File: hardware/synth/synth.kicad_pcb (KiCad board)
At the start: 2 copper layers, 91.4 x 81.3 mm, 54 parts, among them J1 MIDI In, J2 MIDI Out, J3 Audio In, J4 AVR-UPDI-6, J5 Audio Out, SW1 POWER, U1 TLP2312, U2 ATtiny814-SS, U3 MCP6044, U4 MCP6042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

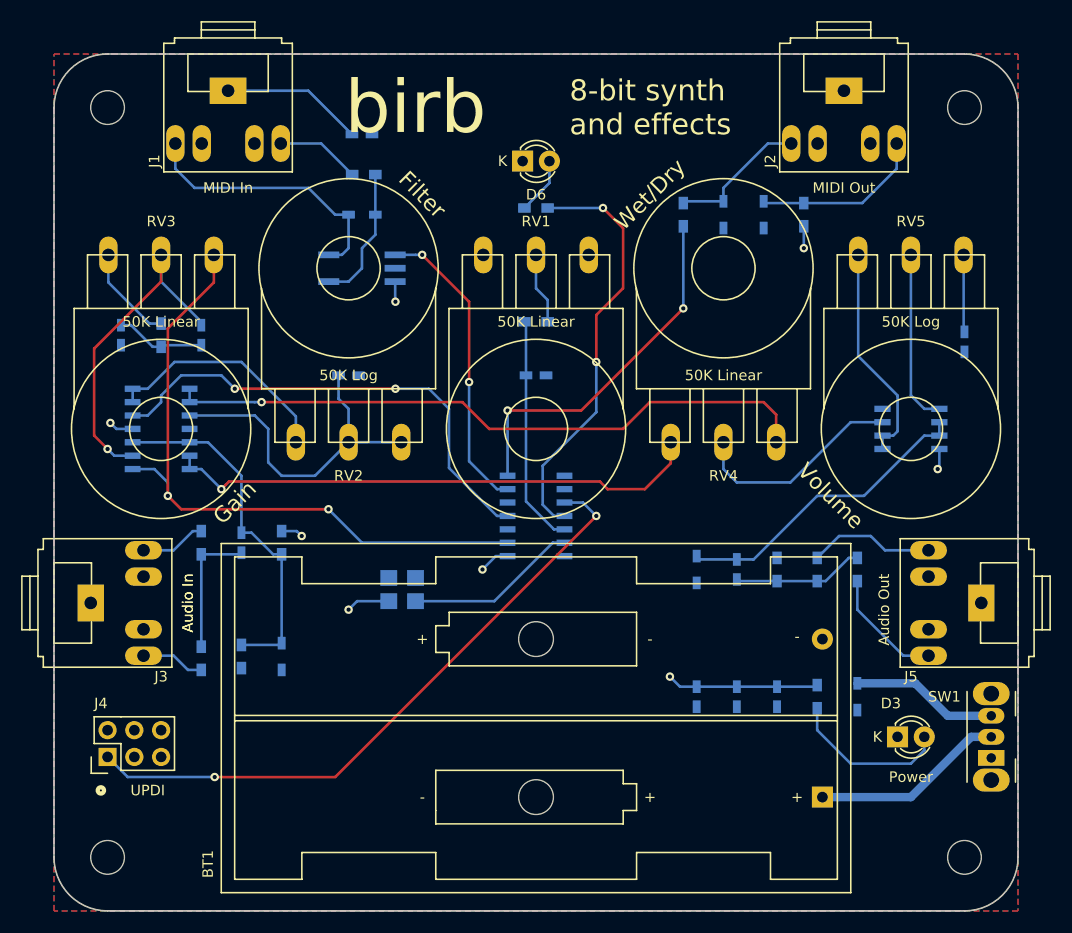
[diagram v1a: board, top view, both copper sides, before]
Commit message: Add selector switch PCB
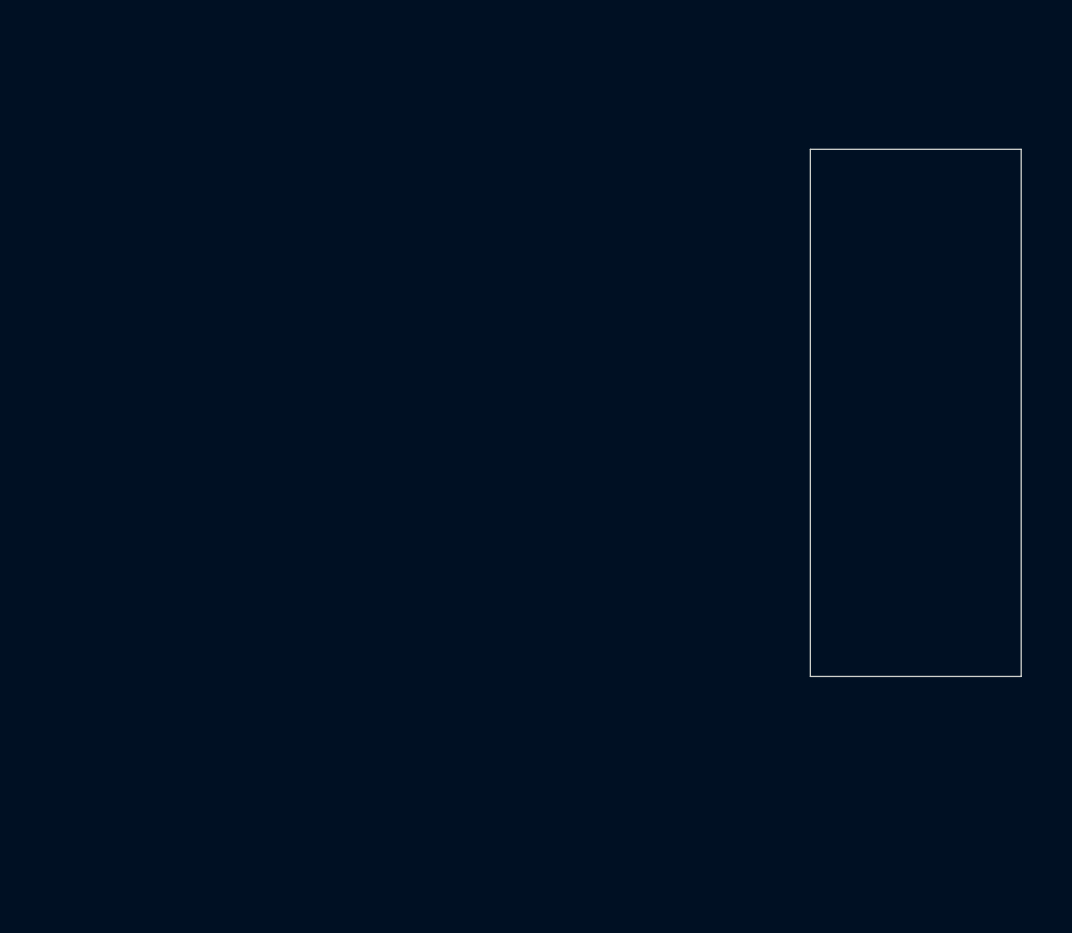
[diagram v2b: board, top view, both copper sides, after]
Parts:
- removed BT1: Battery, Battery:BatteryHolder_Keystone_2462_2xAA
- removed C1: 10u, Capacitors_SMD:C_0603_HandSoldering
- removed C10, C11, C6, C9: 1u, Capacitors_SMD:C_0603_HandSoldering
- removed C2, C4: 100n, Capacitors_SMD:C_0603_HandSoldering
- removed C3: 1n, Capacitors_SMD:C_0603_HandSoldering
- removed C5, C8: DNL, Capacitors_SMD:C_0603_HandSoldering
- removed C7: 10n, Capacitors_SMD:C_0603_HandSoldering
- removed D1, D2, D4, D5, D7, D8: TVS, synth:SOD-323-handsoldering
- removed D3: POWER, LEDs:LED-3MM
- removed D6: LED, LEDs:LED-3MM
- removed J1: MIDI In, synth:Tayda_3.5mm_stereo_TRS_jack_A-853
- removed J2: MIDI Out, synth:Tayda_3.5mm_stereo_TRS_jack_A-853
- removed J3: Audio In, synth:Tayda_3.5mm_stereo_TRS_jack_A-853
- removed J4: AVR-UPDI-6, Pin_Headers:Pin_Header_Straight_2x03
- removed J5: Audio Out, synth:Tayda_3.5mm_stereo_TRS_jack_A-853
- removed R1, R2, R6: 220R, Resistors_SMD:R_0603_HandSoldering
- removed R10, R13, R8: 1M, Resistors_SMD:R_0603_HandSoldering
- removed R11: 100R, Resistors_SMD:R_0603_HandSoldering
- removed R12, R14: 0R, Resistors_SMD:R_0603_HandSoldering
- removed R3, R5: 10R, Resistors_SMD:R_0603_HandSoldering
- removed R4: 100K, Resistors_SMD:R_0603_HandSoldering
- removed R7, R9: 10K, Resistors_SMD:R_0603_HandSoldering
- removed REF** (x4): MountingHole_3.2mm_M3, Mounting_Holes:MountingHole_3.2mm_M3
- removed RV1, RV3, RV4: 50K LIN, synth:Alpha_16mm_Potentiometer_RA
- removed RV2, RV5: 50K LOG, synth:Alpha_16mm_Potentiometer_RA
- removed SW1: POWER, Button_Switch_THT:SW_CuK_OS102011MA1QN1_SPDT_Angled
- removed U1: TLP2312, Package_SO:SO-5_4.4x3.6mm_P1.27mm
- removed U2: ATtiny814-SS, Housings_SOIC:SOIC-14_3.9x8.7mm_Pitch1.27mm
- removed U3: MCP6044, Housings_SOIC:SOIC-14_3.9x8.7mm_Pitch1.27mm
- removed U4: MCP6042, Housings_SOIC:SOIC-8_3.9x4.9mm_Pitch1.27mm
- removed X1: DSC1001, synth:DSC_1001_Oscillator_SMD_5032_4Pads
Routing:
- net /ADC: track 63.9 -> 0.00 mm, vias 2 -> 0
- net Net-(RV4-Pad3): track 62.1 -> 0.00 mm, vias 1 -> 0
- net /UPDI: track 60.9 -> 0.00 mm, vias 2 -> 0
- net Net-(RV4-Pad1): track 51.3 -> 0.00 mm, vias 1 -> 0
- net /DAC: track 46.3 -> 0.00 mm, vias 2 -> 0
- net VDD: track 45.9 -> 0.00 mm, vias 8 -> 0
- net /LED: track 40.4 -> 0.00 mm, vias 2 -> 0
- net /MIDI_OUT: track 34.7 -> 0.00 mm, vias 2 -> 0
- net Net-(C6-Pad1): track 34.0 -> 0.00 mm
- net Net-(C8-Pad1): track 32.4 -> 0.00 mm, vias 1 -> 0
- net Net-(C7-Pad1): track 32.4 -> 0.00 mm
- net Net-(C10-Pad2): track 29.3 -> 0.00 mm
- net /MIDI_IN: track 28.7 -> 0.00 mm, vias 2 -> 0
- net Net-(D2-Pad2): track 25.9 -> 0.00 mm
- net Net-(RV2-Pad1): track 22.4 -> 0.00 mm
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- removed copper zone on B.Cu, net GND
- removed copper zone on F.Cu, net VDD
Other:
- board size 91.4 x 81.3 mm -> 20 x 50 mm
- board text removed: "50K Linear"
- board text removed: "50K Log"
- board text removed: "8-bit synth and effects"
- board text removed: "Audio In"
- board text removed: "Audio Out"
- board text removed: "Filter"
- board text removed: "Gain"
- board text removed: "MIDI In"
- board text removed: "MIDI Out"
- board text removed: "Power"
- board text removed: "R"
- board text removed: "S"
- board text removed: "T"
- board text removed: "UPDI"
- board text removed: "Volume"
- board text removed: "Wet/Dry"
- board text removed: "birb"
- board text removed: "rev 1 by Eric Van Albert"

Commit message: Hardware rev 2 and some firmware updates
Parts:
- added BT1: Battery, Pin_Headers:Pin_Header_Straight_1x02, F.Cu at (122.2, 110.0)
- added C1: 10u, Capacitors_SMD:C_0805_HandSoldering, B.Cu at (131.5, 111.5)
- added C10: 47U, Capacitors_SMD:C_1210_HandSoldering, B.Cu at (136.0, 87.5)
- added C11: 100n, Capacitors_SMD:C_0603_HandSoldering, B.Cu at (122.8, 77.0)
- added C12: 100n, Capacitors_SMD:C_0603_HandSoldering, B.Cu at (132.8, 77.0)
- added C13: 100n, Capacitors_SMD:C_0603_HandSoldering, B.Cu at (122.8, 72.0)
- added C2: 100n, Capacitors_SMD:C_0603_HandSoldering, B.Cu at (127.5, 111.5)
- added C3: 1U, Capacitors_SMD:C_0603_HandSoldering, B.Cu at (133.0, 72.0)
- added C4: 1n, Capacitors_SMD:C_0603_HandSoldering, B.Cu at (129.5, 111.5)
- added C5: 1U, Capacitors_SMD:C_0603_HandSoldering, B.Cu at (125.0, 91.5)
- added C6: DNL, Capacitors_SMD:C_0603_HandSoldering, B.Cu at (132.5, 115.0)
- added C7: 47U, Capacitors_SMD:C_1210_HandSoldering, B.Cu at (124.0, 84.0)
- added C8: 47U, Capacitors_SMD:C_1210_HandSoldering, B.Cu at (124.0, 87.5)
- added C9: 47U, Capacitors_SMD:C_1210_HandSoldering, B.Cu at (136.0, 84.0)
- added D1: TVS, synth:SOD-323-handsoldering, B.Cu at (125.5, 111.3)
- added D2: POWER, LEDs:LED-5MM, F.Cu at (123.5, 106.5)
- added D3: LED, LEDs:LED-5MM, F.Cu at (136.5, 106.5)
- added D4: TVS, synth:SOD-323-handsoldering, B.Cu at (128.8, 88.0)
- added D5: TVS, synth:SOD-323-handsoldering, B.Cu at (131.2, 88.0)
- added D6: TVS, synth:SOD-323-handsoldering, B.Cu at (128.0, 115.0)
- added J1: TTL_MIDI_OUT, Pin_Headers:Pin_Header_Straight_1x01, F.Cu at (138.0, 97.2)
- added J2: MIDI In, Pin_Headers:Pin_Header_Straight_1x03, F.Cu at (127.5, 118.0)
- added J3: Audio Out, Pin_Headers:Pin_Header_Straight_1x03, F.Cu at (127.5, 67.2)
- added J4: UPDI, Pin_Headers:Pin_Header_Straight_1x02, F.Cu at (137.8, 110.0)
- added R1: 22K, Resistors_SMD:R_0603_HandSoldering, B.Cu at (128.5, 83.8)
- added R10: 100K, Resistors_SMD:R_0603_HandSoldering, B.Cu at (127.2, 77.0)
- added R11: 100K, Resistors_SMD:R_0603_HandSoldering, B.Cu at (137.2, 77.0)
- added R12: 100K, Resistors_SMD:R_0603_HandSoldering, B.Cu at (127.2, 72.0)
- added R2: 22K, Resistors_SMD:R_0603_HandSoldering, B.Cu at (131.5, 83.8)
- added R3: 220R, Resistors_SMD:R_0603_HandSoldering, B.Cu at (126.0, 105.2)
- added R4: 220R, Resistors_SMD:R_0603_HandSoldering, B.Cu at (134.2, 105.0)
- added R5: 18K, Resistors_SMD:R_0603_HandSoldering, B.Cu at (123.0, 93.0)
- added R6: 18K, Resistors_SMD:R_0603_HandSoldering, B.Cu at (135.8, 92.0)
- added R7: 220R, Resistors_SMD:R_0603_HandSoldering, B.Cu at (133.5, 111.5)
- added R8: 1M, Resistors_SMD:R_0603_HandSoldering, B.Cu at (127.5, 70.0)
- added R9: 1M, Resistors_SMD:R_0603_HandSoldering, B.Cu at (132.5, 70.0)
- added REF**: MountingHole_2.2mm_M2, Mounting_Holes:MountingHole_2.2mm_M2, F.Cu at (123.0, 117.0)
- added REF**: MountingHole_2.2mm_M2, Mounting_Holes:MountingHole_2.2mm_M2, F.Cu at (123.0, 68.0)
- added REF**: MountingHole_2.2mm_M2, Mounting_Holes:MountingHole_2.2mm_M2, F.Cu at (137.0, 68.0)
- added REF**: MountingHole_2.2mm_M2, Mounting_Holes:MountingHole_2.2mm_M2, F.Cu at (137.0, 117.0)
- added RV1: 50K LOG, Pin_Headers:Pin_Header_Straight_1x03, F.Cu at (133.0, 74.5)
- added RV2: 50K LIN, Pin_Headers:Pin_Header_Straight_1x03, F.Cu at (122.0, 79.5)
- added RV3: 50K LIN, Pin_Headers:Pin_Header_Straight_1x03, F.Cu at (133.0, 79.5)
- added RV4: 50K LIN, Pin_Headers:Pin_Header_Straight_1x03, F.Cu at (122.0, 74.5)
- added U1: TPA6111A2, SMD_Packages:SOIC-8-N, B.Cu at (130.0, 93.0)
- added U2: TLP2312, Package_SO:SO-6_4.4x3.6mm_P1.27mm, B.Cu at (130.0, 104.5)
- added U3: ATtiny1614-SS, SMD_Packages:SOIC-14_N, F.Cu at (130.0, 96.0)
- added X1: DSC1001, synth:DSC_1001_Oscillator_SMD_5032_4Pads, B.Cu at (123.2, 98.8)
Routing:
- net /SELECT: track 0.00 -> 45.2 mm, vias 0 -> 1
- net VDD: track 0.00 -> 39.0 mm, vias 0 -> 4
- net /FREQ: track 0.00 -> 28.2 mm, vias 0 -> 1
- net /UPDI: track 0.00 -> 28.1 mm
- net Net-(C10-Pad1): track 0.00 -> 27.1 mm
- net Net-(C7-Pad1): track 0.00 -> 26.2 mm
- net /DAC: track 0.00 -> 25.0 mm
- net /DEPTH: track 0.00 -> 23.8 mm, vias 0 -> 1
- net /LED: track 0.00 -> 22.2 mm, vias 0 -> 1
- net Net-(C7-Pad2): track 0.00 -> 21.0 mm
- net Net-(R1-Pad1): track 0.00 -> 17.9 mm, vias 0 -> 2
- net /MIDI_IN: track 0.00 -> 17.8 mm, vias 0 -> 1
- net Net-(C10-Pad2): track 0.00 -> 17.5 mm
- net Net-(D6-Pad2): track 0.00 -> 16.5 mm, vias 0 -> 2
- net Net-(D6-Pad1): track 0.00 -> 15.8 mm
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- added copper zone on B.Cu, net GND
- added copper zone on F.Cu, net VDD
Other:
- board size 20 x 50 mm -> 20 x 55 mm
- net class Default removed
- board text added: "+ -"
- board text added: "5 4 2"
- board text added: "8-bit synth"
- board text added: "Audio Out"
- board text added: "Depth"
- board text added: "Frequency"
- board text added: "Gnd"
- board text added: "MIDI In"
- board text added: "Power"
- board text added: "Power LED"
- board text added: "Prog Out"
- board text added: "Select"
- board text added: "Synth LED"
- board text added: "T R S"
- board text added: "UPDI"
- board text added: "Volume"
- board text added: "birb"
- board text added: "rev 2 by Eric Van Albert"

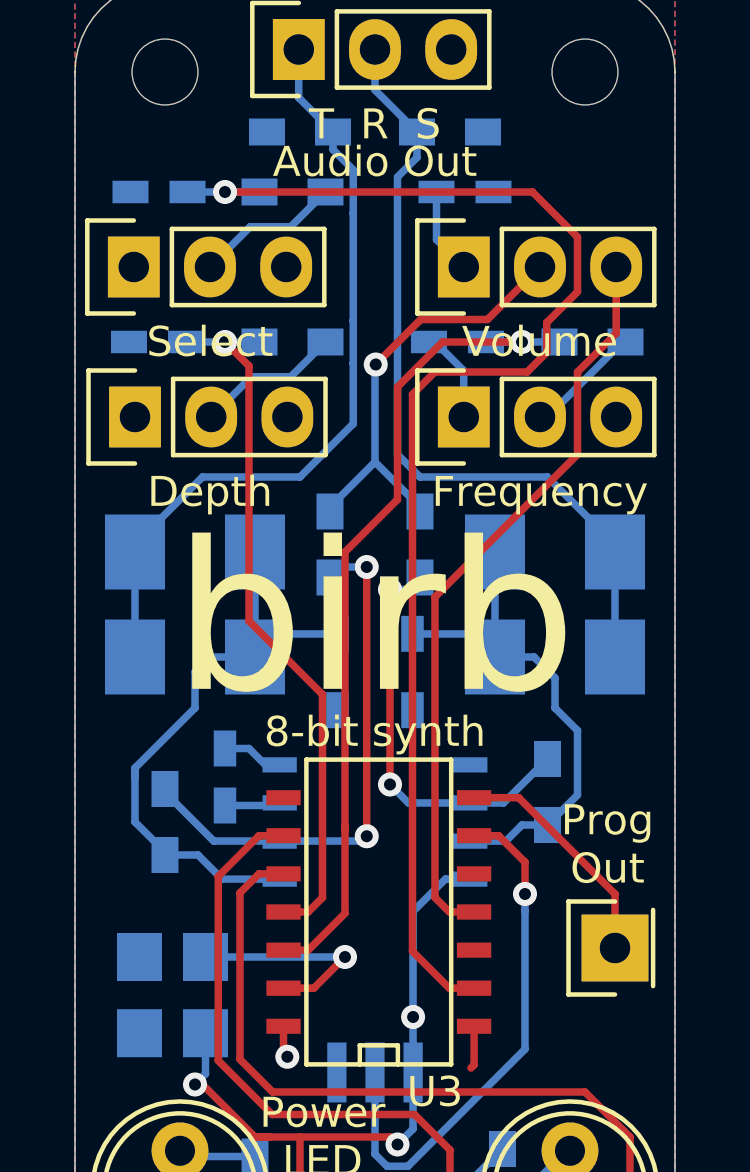
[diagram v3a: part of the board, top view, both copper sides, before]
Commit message: Update synth board to rev3 (fixing volume control) and selector switch to rev2
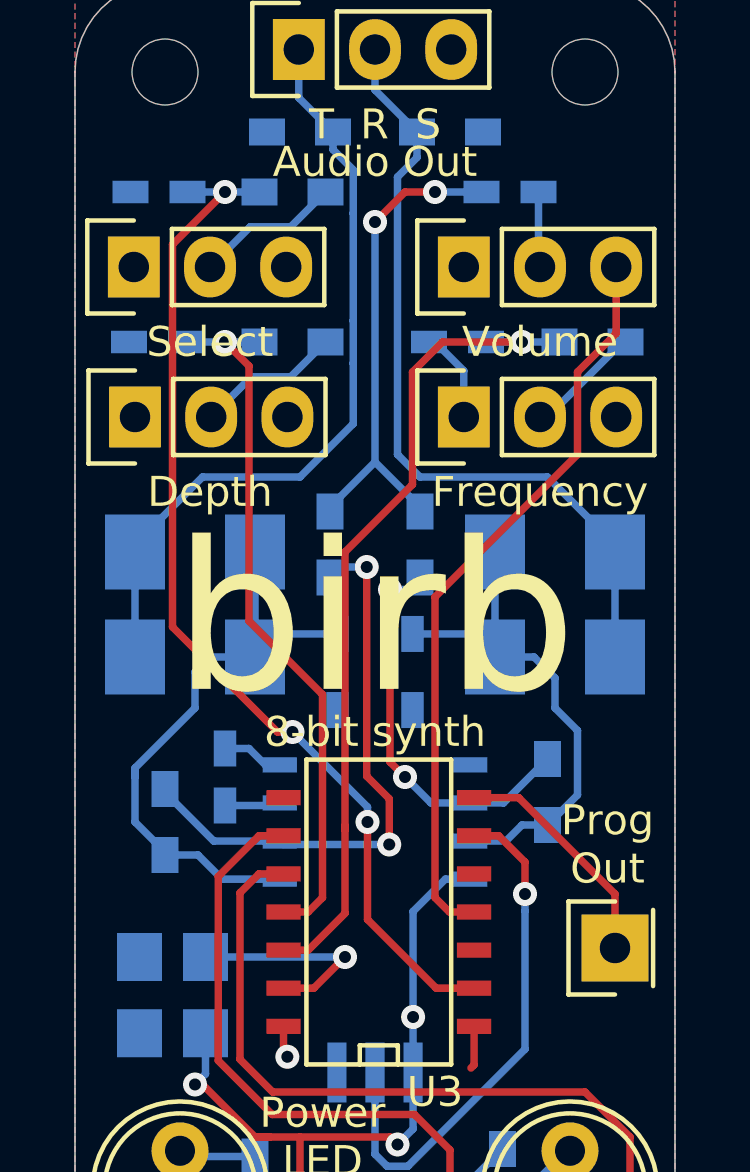
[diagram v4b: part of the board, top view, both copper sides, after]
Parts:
- R8, R9: value 1M -> 10K
- moved C3 1.50 mm to (134.5, 72.0), turned to 180 degrees
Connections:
- C3 pad 2: GND -> Net-(R1-Pad2)
- RV1 pad 1: Net-(C3-Pad1) -> GND
- RV1 pad 2: Net-(R1-Pad2) -> Net-(C3-Pad1)
- U3 pad 3: Net-(U3-Pad3) -> unconnected-(U3-Pad3)
- U3 pad 5: Net-(U3-Pad5) -> unconnected-(U3-Pad5)
- U3 pad 8: Net-(U3-Pad8) -> unconnected-(U3-Pad8)
- X1 pad 1: Net-(X1-Pad1) -> unconnected-(X1-Pad1)
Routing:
- net /SELECT: track 45.2 -> 34.9 mm, vias 1 -> 3
- net Net-(R1-Pad2): track 14.6 -> 16.5 mm, vias 1 -> 2
- net Net-(R1-Pad1): track 17.9 -> 19.2 mm
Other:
- board text added: "rev 3 by Eric Van Albert"
- board text removed: "rev 2 by Eric Van Albert"
